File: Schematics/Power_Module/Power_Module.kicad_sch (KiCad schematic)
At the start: 33 parts, among them J1 Screw_Terminal_01x02, J2 Screw_Terminal_01x02, J3 Screw_Terminal_01x02, J4 Screw_Terminal_01x02, Q1 PMOS, Q2 PMOS, U1 LMR51430XDDCR, U2 LMR51430XDDCR, U3 LMR51430XDDCR

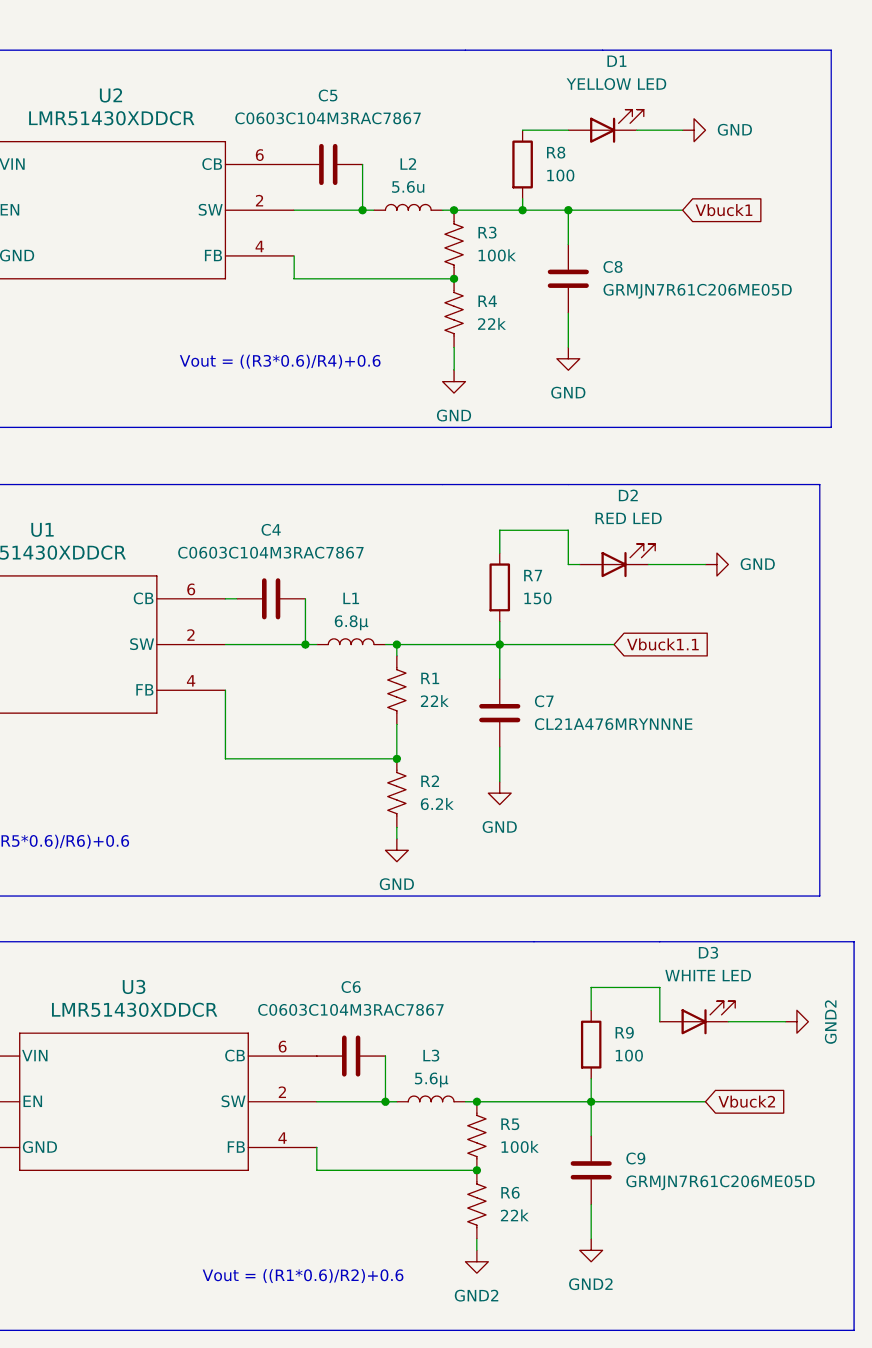
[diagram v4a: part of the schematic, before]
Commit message: All values displayed
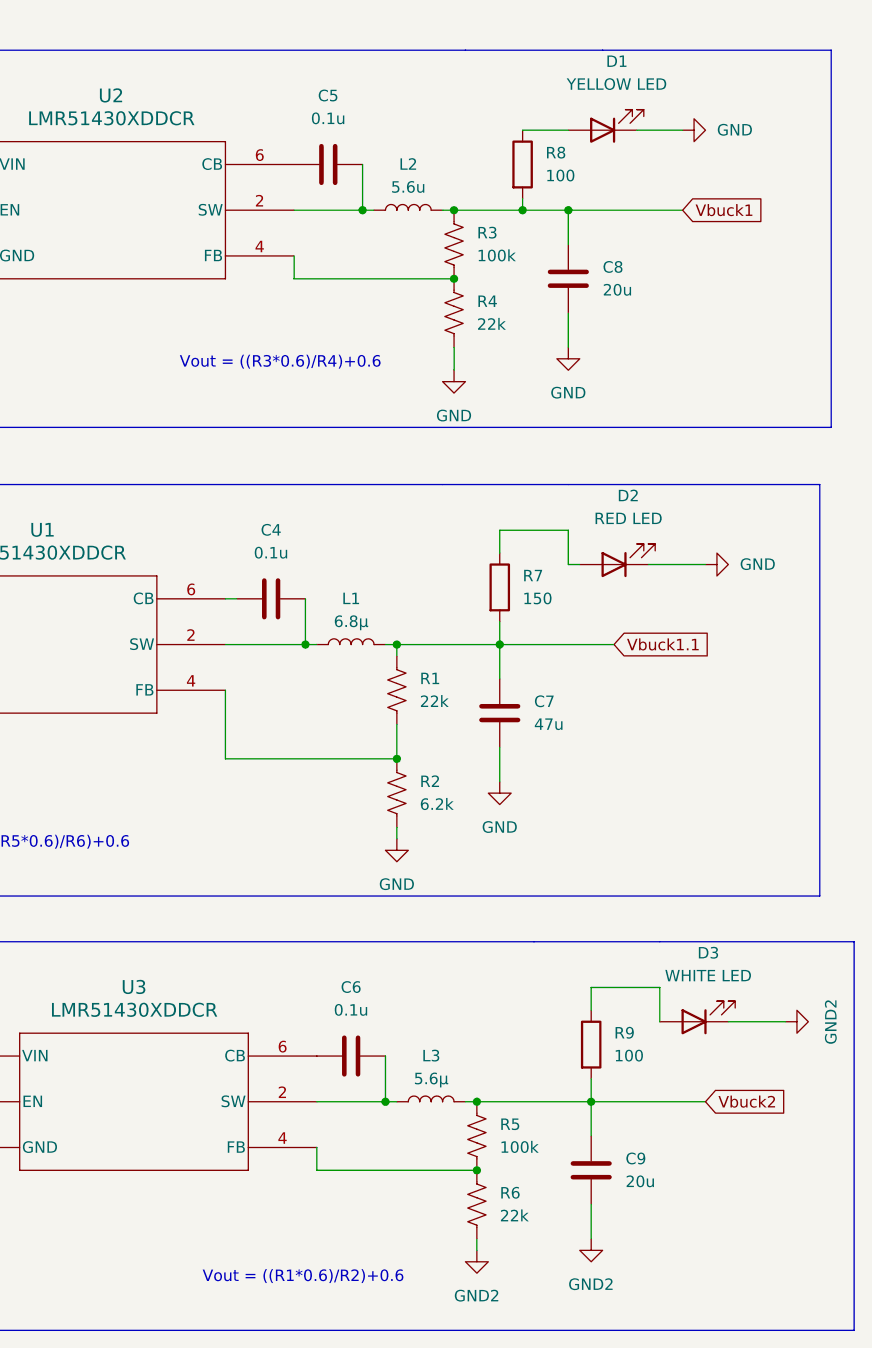
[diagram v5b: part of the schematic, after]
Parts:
- C4, C5, C6: value C0603C104M3RAC7867 -> 0.1u; Part # (none) -> C0603C104M3RAC7867
- C7: value CL21A476MRYNNNE -> 47u; LCSC (none) -> C2185054
- C8, C9: value GRMJN7R61C206ME05D -> 20u; Part # (none) -> GRMJN7R61C206ME05D
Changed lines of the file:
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@@
       (effects (font (size 1.27 1.27)) (justify left))
     )
-    (property "Value" "GRMJN7R61C206ME05D" (at 208.28 49.53 0)
+    (property "Value" "20u" (at 208.28 49.53 0)
       (effects (font (size 1.27 1.27)) (justify left))
     )
@@
       (effects (font (size 1.27 1.27)) hide)
     )
+    (property "Part #" "GRMJN7R61C206ME05D" (at 204.47 48.26 0)
+      (effects (font (size 1.27 1.27)) hide)
+    )
     (pin "1")
     (pin "2")
@@
       (effects (font (size 1.27 1.27)))
     )
-    (property "Value" "C0603C104M3RAC7867" (at 177.8 30.48 90)
+    (property "Value" "0.1u" (at 177.8 30.48 90)
       (effects (font (size 1.27 1.27)))
     )
@@
       (effects (font (size 1.27 1.27)) hide)
     )
+    (property "Part #" "C0603C104M3RAC7867" (at 177.8 35.56 90)
+      (effects (font (size 1.27 1.27)) hide)
+    )
     (pin "1")
     (pin "2")
@@
       (effects (font (size 1.27 1.27)) (justify left))
     )
-    (property "Value" "GRMJN7R61C206ME05D" (at 210.82 148.59 0)
+    (property "Value" "20u" (at 210.82 148.59 0)
       (effects (font (size 1.27 1.27)) (justify left))
     )
@@
     )
     (property "Datasheet" "~" (at 207.01 147.32 0)
+      (effects (font (size 1.27 1.27)) hide)
+    )
+    (property "Part #" "GRMJN7R61C206ME05D" (at 207.01 147.32 0)
       (effects (font (size 1.27 1.27)) hide)
     )
@@
       (effects (font (size 1.27 1.27)))
     )
-    (property "Value" "C0603C104M3RAC7867" (at 171.45 78.74 90)
+    (property "Value" "0.1u" (at 171.45 78.74 90)
       (effects (font (size 1.27 1.27)))
     )
@@
       (effects (font (size 1.27 1.27)) hide)
     )
+    (property "Part #" "C0603C104M3RAC7867" (at 171.45 83.82 90)
+      (effects (font (size 1.27 1.27)) hide)
+    )
     (pin "1")
     (pin "2")
@@
       (effects (font (size 1.27 1.27)))
     )
-    (property "Value" "C0603C104M3RAC7867" (at 180.34 129.54 90)
+    (property "Value" "0.1u" (at 180.34 129.54 90)
       (effects (font (size 1.27 1.27)))
     )
@@
       (effects (font (size 1.27 1.27)) hide)
     )
+    (property "Part #" "C0603C104M3RAC7867" (at 180.34 134.62 90)
+      (effects (font (size 1.27 1.27)) hide)
+    )
     (pin "1")
     (pin "2")
@@
       (effects (font (size 1.27 1.27)) (justify left))
     )
-    (property "Value" "CL21A476MRYNNNE" (at 200.66 97.79 0)
+    (property "Value" "47u" (at 200.66 97.79 0)
       (effects (font (size 1.27 1.27)) (justify left))
     )
@@
       (effects (font (size 1.27 1.27)) hide)
     )
+    (property "LCSC" "C2185054" (at 196.85 96.52 0)
+      (effects (font (size 1.27 1.27)) hide)
+    )

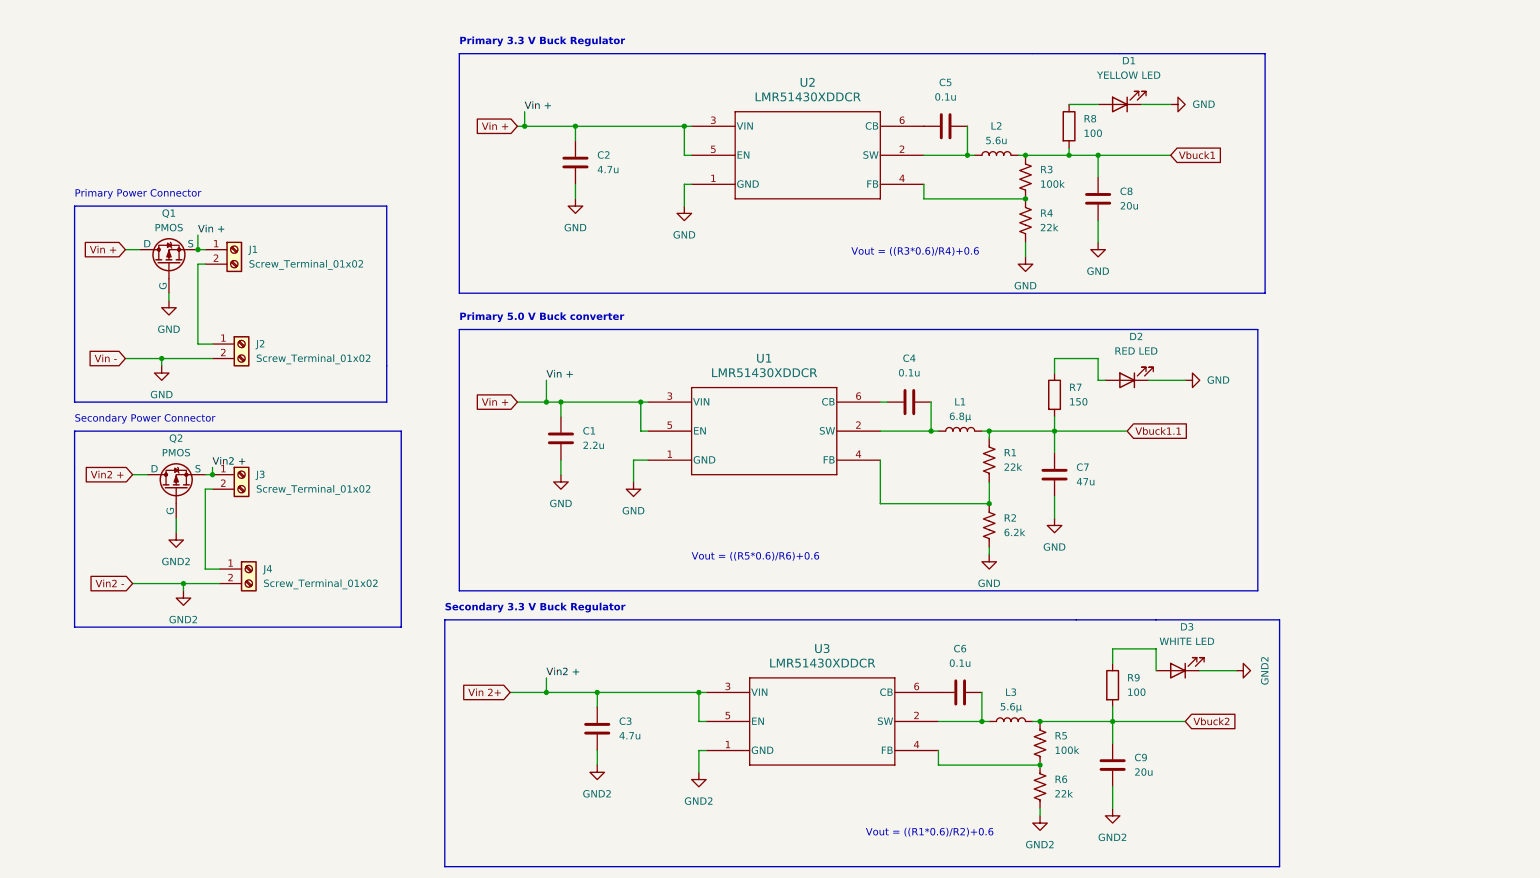
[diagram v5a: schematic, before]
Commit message: Added stack edge connector
Added stack edge connector
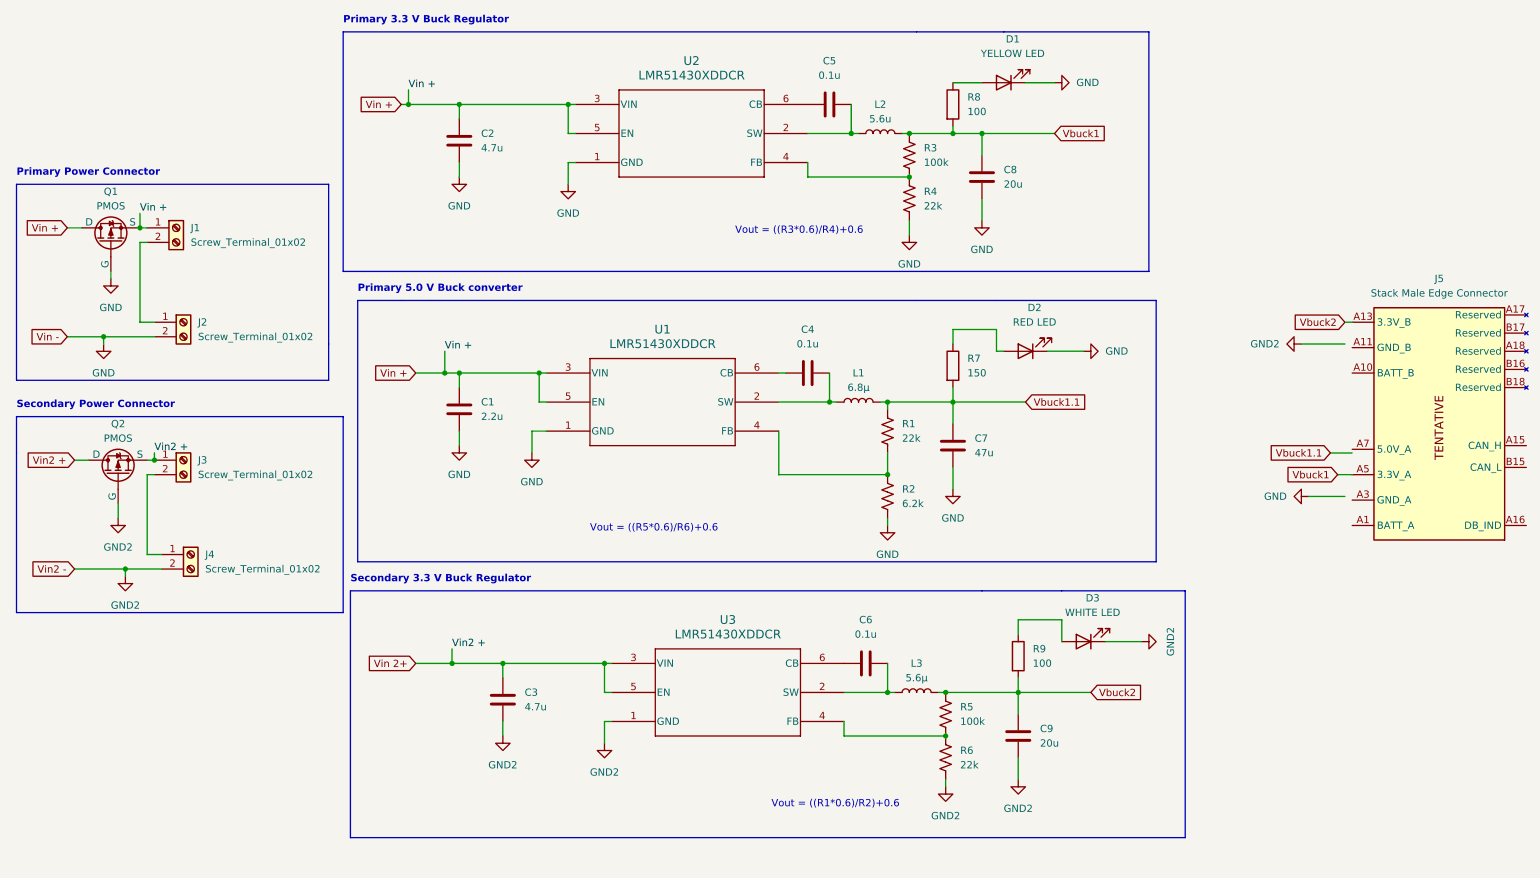
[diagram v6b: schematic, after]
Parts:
- added J5: Stack Male Edge Connector, Connector_PCBEdge:BUS_PCIexpress_x1, symbol EdgeConnector:Stack Male Edge Connector
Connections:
- net Vbuck1: now also J5.A5 (3.3V_A), J5.B5 (3.3V_A)
- net Vbuck2: now also J5.A13 (3.3V_B), J5.B13 (3.3V_B)
- new net: J5.A1 (BATT_A), J5.A2 (BATT_A), J5.B1 (BATT_A), J5.B2 (BATT_A)
- new net: J5.A10 (BATT_B), J5.A9 (BATT_B), J5.B10 (BATT_B), J5.B9 (BATT_B)
- new net: J5.A11 (GND_B), J5.A12 (GND_B), J5.A14 (GND_B), J5.B11 (GND_B), J5.B12 (GND_B), J5.B14 (GND_B)
- new net: J5.A3 (GND_A), J5.A4 (GND_A), J5.A6 (GND_A), J5.A8 (GND_A), J5.B3 (GND_A), J5.B4 (GND_A), J5.B6 (GND_A), J5.B8 (GND_A)
- new net: J5.A7 (5.0V_A), J5.B7 (5.0V_A)
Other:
- moved on the sheet: C1, C2, C3, C4, C5, C6, C7, C8, C9, D1, D2, D3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

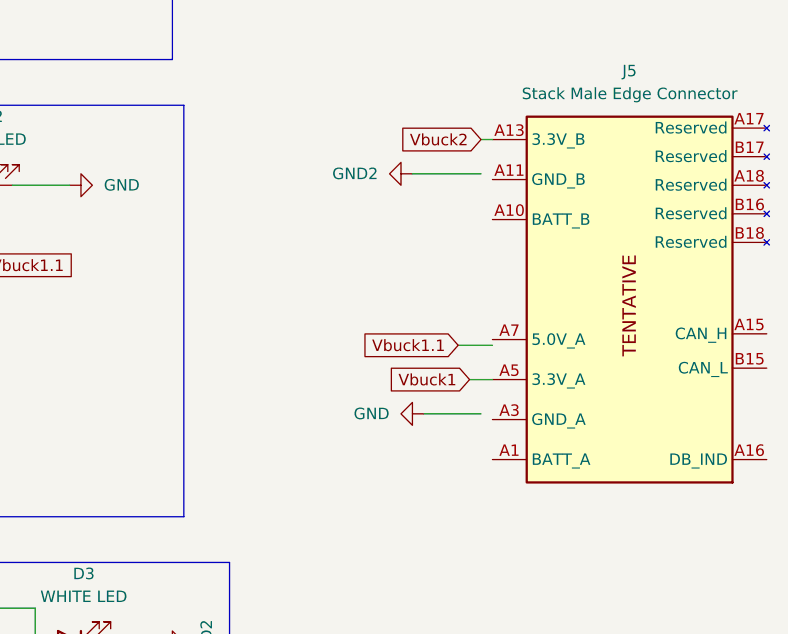
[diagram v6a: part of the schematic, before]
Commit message: Fixed stack edge connector connections
Fixed stack edge connector connections
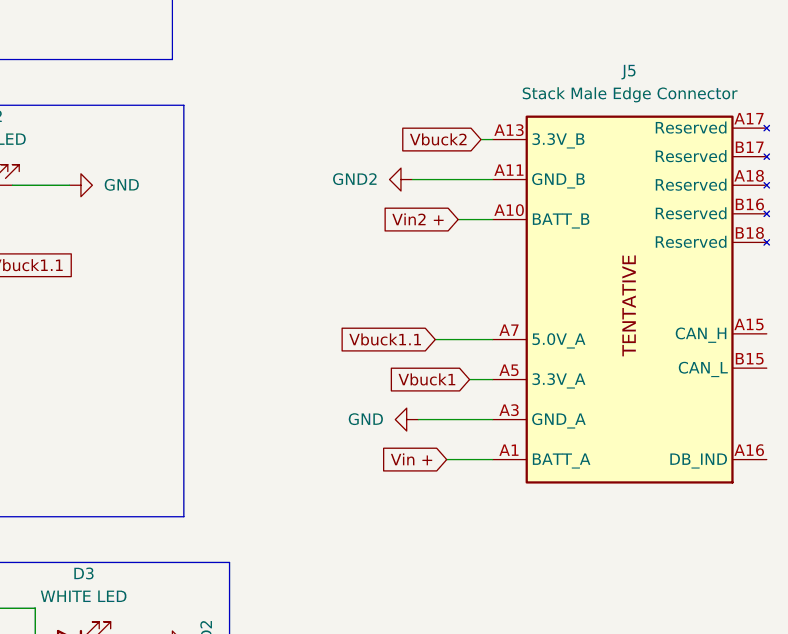
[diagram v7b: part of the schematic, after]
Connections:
- net GND: now also J5.A3 (GND_A), J5.A4 (GND_A), J5.A6 (GND_A), J5.A8 (GND_A), J5.B3 (GND_A), J5.B4 (GND_A), J5.B6 (GND_A), J5.B8 (GND_A)
- net GND2: now also J5.A11 (GND_B), J5.A12 (GND_B), J5.A14 (GND_B), J5.B11 (GND_B), J5.B12 (GND_B), J5.B14 (GND_B)
- net Vbuck1.1: now also J5.A7 (5.0V_A), J5.B7 (5.0V_A)
- net Vin +: now also J5.A1 (BATT_A), J5.A2 (BATT_A), J5.B1 (BATT_A), J5.B2 (BATT_A)
- net Vin 2+: now also J5.A10 (BATT_B), J5.A9 (BATT_B), J5.B10 (BATT_B), J5.B9 (BATT_B)
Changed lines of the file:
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@@
   (junction (at 91.44 129.54) (diameter 0) (color 0 0 0 0)
   )
-  (wire (pts (xy 240.03 73.66) (xy 247.65 73.66))
+  (wire (pts (xy 240.03 74.295) (xy 248.92 74.295))
     (stroke (width 0) (type default))
   )
@@
     (stroke (width 0) (type default))
   )
+  (wire (pts (xy 245.11 78.74) (xy 248.92 78.74))
+    (stroke (width 0) (type default))
+  )
+  (wire (pts (xy 243.84 105.41) (xy 248.92 105.41))
+    (stroke (width 0) (type default))
+  )
   (wire (pts (xy 160.02 134.62) (xy 167.64 134.62))
     (stroke (width 0) (type default))
@@
     (stroke (width 0) (type default))
   )
-  (wire (pts (xy 245.11 92.71) (xy 248.92 92.71))
+  (wire (pts (xy 242.57 92.075) (xy 248.92 92.075))
     (stroke (width 0) (type default))
   )
@@
     (stroke (width 0) (type default))
   )
+  (wire (pts (xy 240.665 100.965) (xy 248.92 100.965))
+    (stroke (width 0) (type default))
+  )
   (polyline (pts (xy 219.71 160.02) (xy 219.71 116.84))
     (stroke (width 0) (type default))
@@
   )
   (wire (pts (xy 148.59 96.52) (xy 167.64 96.52))
-    (stroke (width 0) (type default))
-  )
-  (wire (pts (xy 241.3 100.33) (xy 247.65 100.33))
     (stroke (width 0) (type default))
   )
@@
     )
   )
+  (global_label "Vin2 +" (shape input) (at 245.11 78.74 180) (fields_autoplaced)
+    (effects (font (size 1.27 1.27)) (justify right))
+    (property "Intersheetrefs" "${INTERSHEET_REFS}" (at 235.5329 78.74 0)
+      (effects (font (size 1.27 1.27)) (justify right) hide)
+    )
+  )
   (global_label "Vbuck2" (shape input) (at 203.2 134.62 0) (fields_autoplaced)
     (effects (font (size 1.27 1.27)) (justify left))
@@
     )
   )
+  (global_label "Vin +" (shape input) (at 243.84 105.41 180) (fields_autoplaced)
+    (effects (font (size 1.27 1.27)) (justify right))
+    (property "Intersheetrefs" "${INTERSHEET_REFS}" (at 235.4724 105.41 0)
+      (effects (font (size 1.27 1.27)) (justify right) hide)
+    )
+  )
   (global_label "Vin -" (shape input) (at 24.13 72.39 180) (fields_autoplaced)
     (effects (font (size 1.27 1.27)) (justify right))
@@
     )
   )
-  (global_label "Vbuck1.1" (shape input) (at 245.11 92.71 180) (fields_autoplaced)
+  (global_label "Vbuck1.1" (shape input) (at 242.57 92.075 180) (fields_autoplaced)
     (effects (font (size 1.27 1.27)) (justify right))
-    (property "Intersheetrefs" "${INTERSHEET_REFS}" (at 233.5977 92.71 0)
+    (property "Intersheetrefs" "${INTERSHEET_REFS}" (at 231.0577 92.075 0)
       (effects (font (size 1.27 1.27)) (justify right) hide)
     )
@@
     )
   )
-  (symbol (lib_id "power:GND2") (at 240.03 73.66 270) (unit 1)
-    (in_bom yes) (on_board yes) (dnp no) (fields_autoplaced)
-    (property "Reference" "#PWR020" (at 233.68 73.66 0)
-      (effects (font (size 1.27 1.27)) hide)
-    )
-    (property "Value" "GND2" (at 236.22 73.66 90)
+  (symbol (lib_id "power:GND2") (at 240.03 74.295 270) (unit 1)
+    (in_bom yes) (on_board yes) (dnp no) (fields_autoplaced)
+    (property "Reference" "#PWR020" (at 233.68 74.295 0)
+      (effects (font (size 1.27 1.27)) hide)
+    )
+    (property "Value" "GND2" (at 236.22 74.295 90)
       (effects (font (size 1.27 1.27)) (justify right))
     )
-    (property "Footprint" "" (at 240.03 73.66 0)
-      (effects (font (size 1.27 1.27)) hide)
-    )
-    (property "Datasheet" "" (at 240.03 73.66 0)
+    (property "Footprint" "" (at 240.03 74.295 0)
+      (effects (font (size 1.27 1.27)) hide)
+    )
+    (property "Datasheet" "" (at 240.03 74.295 0)
       (effects (font (size 1.27 1.27)) hide)
     )
@@
     )
   )
-  (symbol (lib_id "power:GND") (at 241.3 100.33 270) (unit 1)
-    (in_bom yes) (on_board yes) (dnp no) (fields_autoplaced)
-    (property "Reference" "#PWR021" (at 234.95 100.33 0)
-      (effects (font (size 1.27 1.27)) hide)
-    )
-    (property "Value" "GND" (at 237.49 100.33 90)
+  (symbol (lib_id "power:GND") (at 240.665 100.965 270) (unit 1)
+    (in_bom yes) (on_board yes) (dnp no) (fields_autoplaced)
+    (property "Reference" "#PWR021" (at 234.315 100.965 0)
+      (effects (font (size 1.27 1.27)) hide)
+    )
+    (property "Value" "GND" (at 236.855 100.965 90)
       (effects (font (size 1.27 1.27)) (justify right))
     )
-    (property "Footprint" "" (at 241.3 100.33 0)
-      (effects (font (size 1.27 1.27)) hide)
-    )
-    (property "Datasheet" "" (at 241.3 100.33 0)
-      (effects (font (size 1.27 1.27)) hide)
-    )
+    (property "Footprint" "" (at 240.665 100.965 0)
+      (effects (font (size 1.27 1.27)) hide)
+    )
+    (property "Datasheet" "" (at 240.665 100.965 0)
+      (effects (font (size 1.27 1.27)) hide)
+    )
